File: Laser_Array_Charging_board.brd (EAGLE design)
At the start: 80 x 90 mm, 16 parts, among them X1 1751248, X3 22-23-2031, X4 22-23-2041

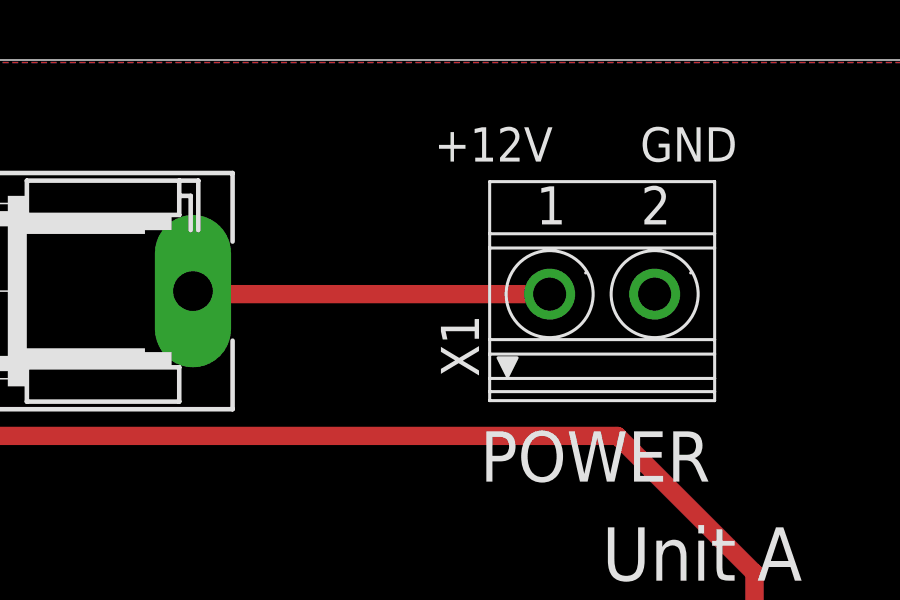
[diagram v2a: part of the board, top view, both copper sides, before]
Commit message: Charging Board  header change, V1.1, again
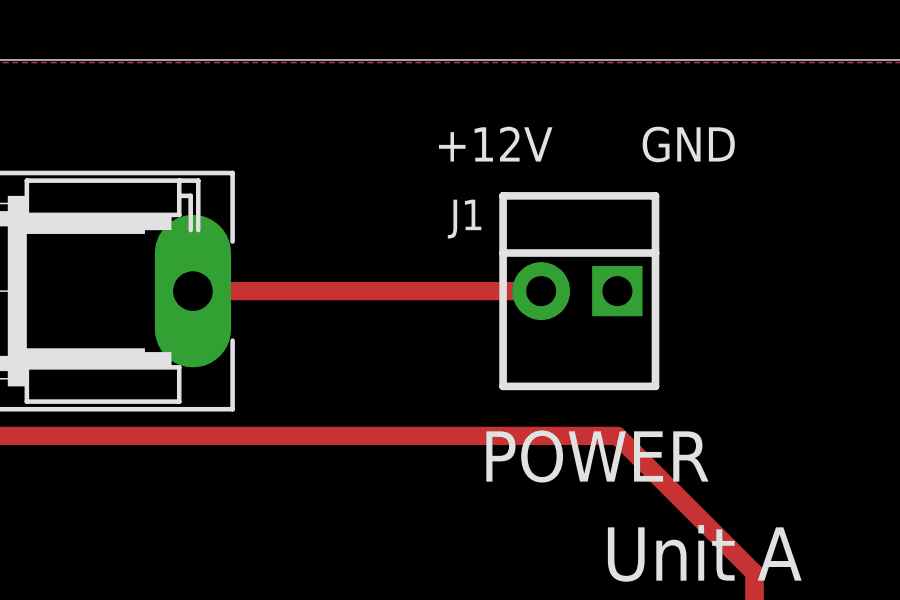
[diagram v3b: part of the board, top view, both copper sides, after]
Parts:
- removed X1: 1751248, con-phoenix-350:1751248
- added J1: 22-23-2021, Mine:22-23-2021
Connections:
- net +12V_TB: now also J1.1; no longer X1.1
- net GND: now also J1.2; no longer X1.2
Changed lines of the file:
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@@
 <attribute name="NAME" x="72.263" y="55.372" size="1.27" layer="25" rot="R180"/>
-</element>
-<element name="X1" library="con-phoenix-350" package="1751248" value="1751248" x="54.864" y="82.296" smashed="yes">
-<attribute name="OC_FARNELL" value="unknown" x="54.864" y="82.296" size="1.778" layer="27" display="off"/>
-<attribute name="OC_NEWARK" value="unknown" x="54.864" y="82.296" size="1.778" layer="27" display="off"/>
-<attribute name="MPN" value="" x="54.864" y="82.296" size="1.778" layer="27" display="off"/>
-<attribute name="MF" value="" x="54.864" y="82.296" size="1.778" layer="27" display="off"/>
-<attribute name="NAME" x="50.759" y="79.4385" size="1.27" layer="25" rot="R90"/>
 </element>
 <element name="X3" library="Mine" package="22-23-2031" value="22-23-2031" x="55.88" y="9.906" smashed="yes" rot="R180">
@@
 <attribute name="OC_FARNELL" value="1462920" x="30.734" y="9.144" size="1.778" layer="27" rot="R180" display="off"/>
 <attribute name="NAME" x="38.354" y="7.112" size="1.016" layer="25" ratio="10" rot="R180"/>
+</element>
+<element name="J1" library="Mine" package="22-23-2021" value="22-23-2021" x="54.102" y="82.296" smashed="yes">
+<attribute name="OC_FARNELL" value="1462926" x="54.102" y="82.296" size="1.778" layer="27" display="off"/>
+<attribute name="MPN" value="22-23-2021" x="54.102" y="82.296" size="1.778" layer="27" display="off"/>
+<attribute name="OC_NEWARK" value="25C3832" x="54.102" y="82.296" size="1.778" layer="27" display="off"/>
+<attribute name="MF" value="MOLEX" x="54.102" y="82.296" size="1.778" layer="27" display="off"/>
+<attribute name="NAME" x="49.784" y="84.328" size="1.016" layer="25" ratio="10"/>
 </element>
 </elements>
@@
 <contactref element="R3" pad="1"/>
 <contactref element="R6" pad="1"/>
-<contactref element="X1" pad="2"/>
 <contactref element="THR1" pad="2"/>
 <contactref element="THR2" pad="2"/>
@@
 <contactref element="CHG2" pad="5"/>
 <contactref element="R1" pad="1"/>
+<contactref element="J1" pad="2"/>
 </signal>
 <signal name="N$1">
@@
 </signal>
 <signal name="+12V_TB">
-<contactref element="X1" pad="1"/>
 <contactref element="F2" pad="2"/>
-<wire x1="53.114" y1="82.196" x2="41.2242" y2="82.196" width="0.6096" layer="1"/>
 <wire x1="41.2242" y1="82.196" x2="41.2242" y2="82.296" width="0.6096" layer="1"/>
+<contactref element="J1" pad="1"/>
+<wire x1="41.2242" y1="82.296" x2="52.832" y2="82.296" width="0.6096" layer="1"/>
 </signal>
 </signals>

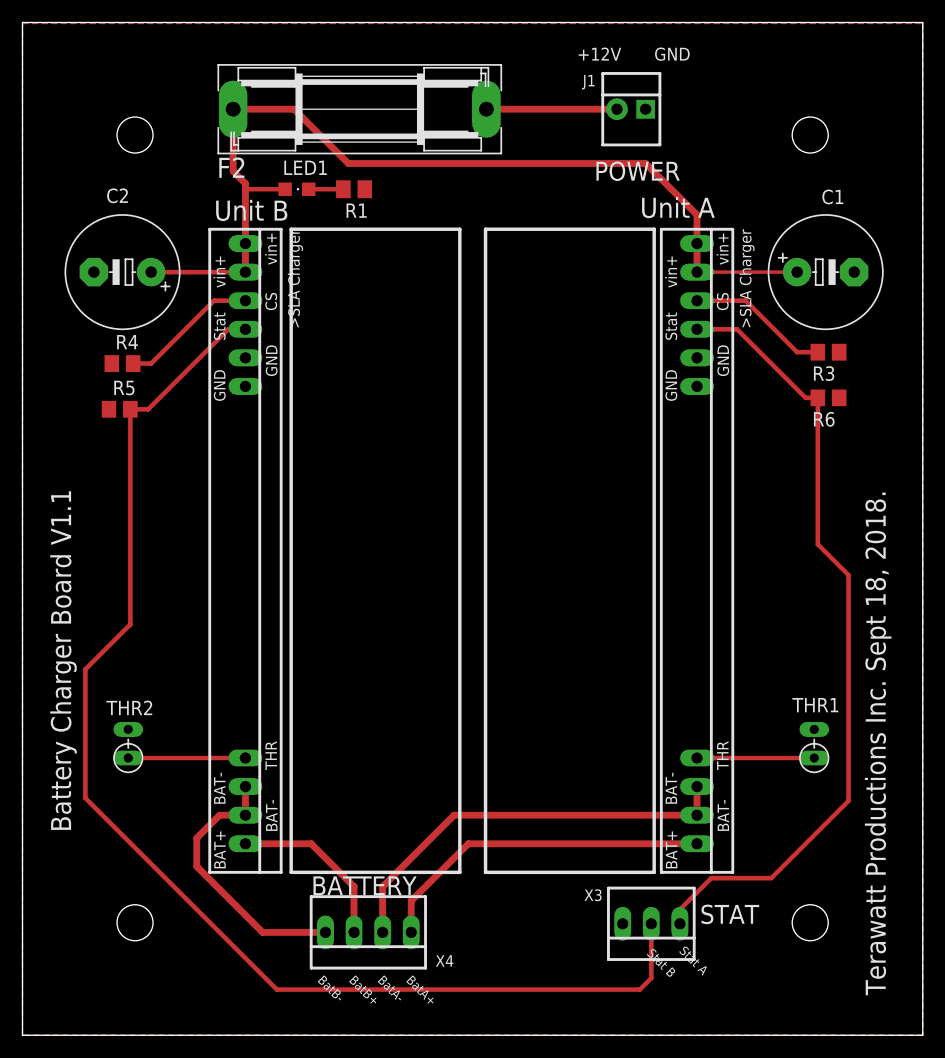
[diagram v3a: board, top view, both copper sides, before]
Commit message: Finished Laser_Array next versions, all three boards including revised charger board
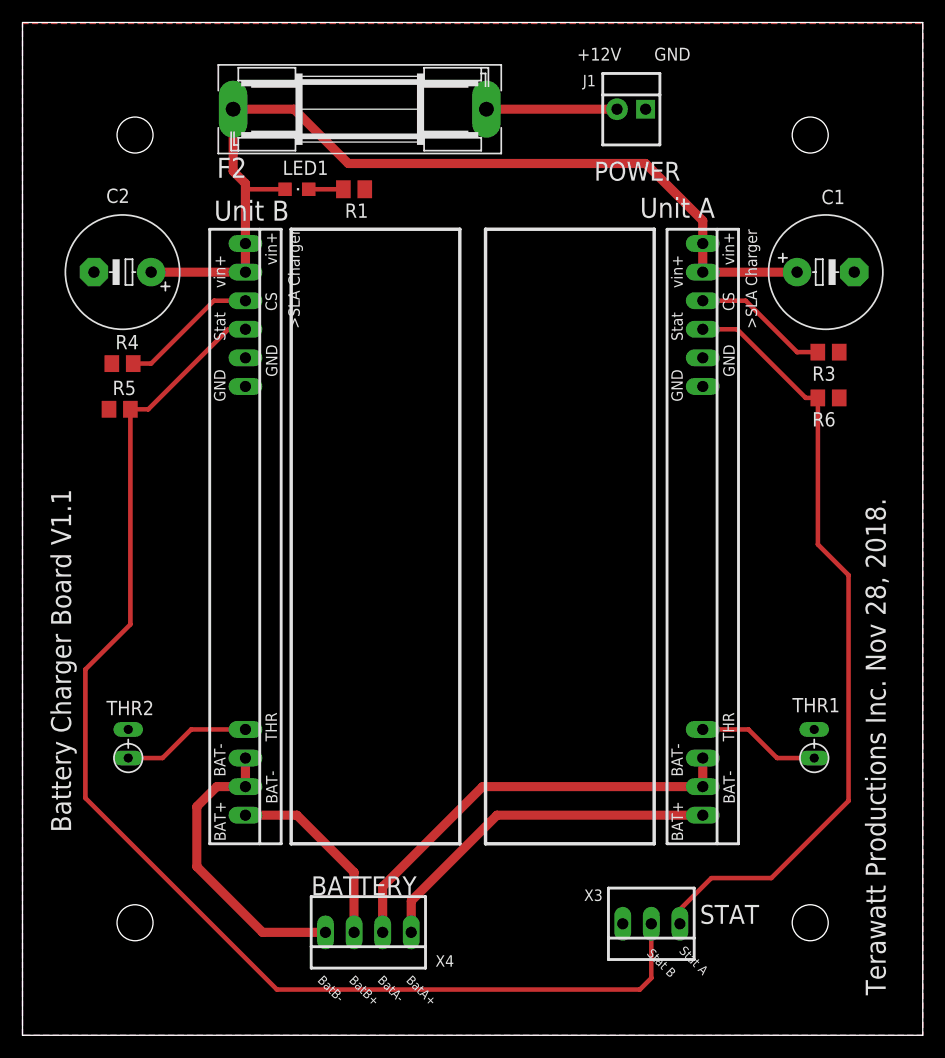
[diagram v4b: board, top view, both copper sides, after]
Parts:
- moved CHG1 0.51 mm to (60.5, 47.5)
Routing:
- net BATB_-: track 24.1 -> 26.8 mm
- net BATB_+: track 15.3 -> 17.1 mm
- net BATA_-: track 37.2 -> 38.7 mm
- net BATA_+: track 30.3 -> 31.9 mm
- net N$2: track 10.4 -> 11.5 mm
- net N$1: track 10.4 -> 11.0 mm
- net STAT1: track 70.5 -> 69.9 mm
- net N$7: track 12.6 -> 12.1 mm
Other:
- board text added: "Terawatt Productions Inc. Nov 28, 2018."
- board text removed: "Terawatt Productions Inc. Sept 18, 2018."
